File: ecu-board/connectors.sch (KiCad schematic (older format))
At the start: 31 parts, among them J10 Injector connector, J13 Chrankshaft Hall connector, J14 Camshaft Hall connector, J2 Battery power conenctor, J4 Motor conenctor, J5 Serial DB9 connector, J8 IAT connector, J9 CLT connector

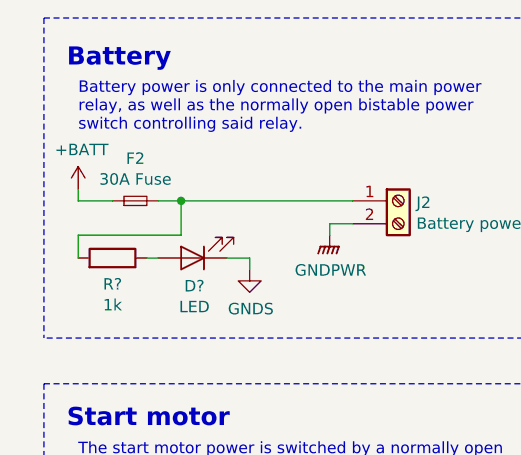
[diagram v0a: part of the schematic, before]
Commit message: Remove main fuse. To be replaced by inline. See #4.
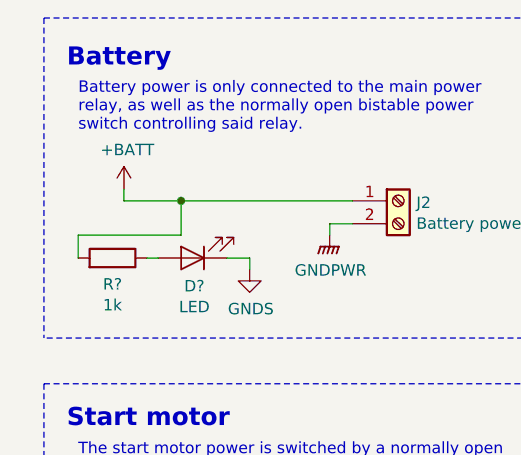
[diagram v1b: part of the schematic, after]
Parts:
- removed F2: 30A Fuse, symbol Device:Fuse_Small
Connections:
- net +BATT: now also J2.1 (Pin_1), R?.2
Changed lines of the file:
@@
 L power:+BATT #PWR06
 U 1 1 5C5D2F4D
-P 950 1650
-F 0 "#PWR06" H 950 1500 50  0001 C CNN
-F 1 "+BATT" H 965 1823 50  0000 C CNN
-F 2 "" H 950 1650 50  0001 C CNN
-F 3 "" H 950 1650 50  0001 C CNN
-	1    950  1650
+P 1150 1650
+F 0 "#PWR06" H 1150 1500 50  0001 C CNN
+F 1 "+BATT" H 1165 1823 50  0000 C CNN
+F 2 "" H 1150 1650 50  0001 C CNN
+F 3 "" H 1150 1650 50  0001 C CNN
+	1    1150 1650
 	1    0    0    -1
 $EndComp
 Wire Wire Line
 	2050 1800 2150 1800
-$Comp
-L Device:Fuse_Small F2
-U 1 1 5C5D4B6E
-P 1200 1700
-F 0 "F2" H 1200 1515 50  0000 C CNN
-F 1 "30A Fuse" H 1200 1606 50  0000 C CNN
-F 2 "" H 1200 1700 50  0001 C CNN
-F 3 "~" H 1200 1700 50  0001 C CNN
-F 4 "2292904" H -5600 -2800 50  0001 C CNN "Farnell"
-	1    1200 1700
-	1    0    0    1
-$EndComp
 Wire Notes Line
 	3400 2300 800  2300
@@
 	1650 3700 1700 3700
 Wire Wire Line
-	950  1650 950  1700
-Wire Wire Line
-	950  1700 1100 1700
+	1150 1650 1150 1700
 Wire Wire Line
 	1900 3300 2000 3300
@@
 	1    0    0    -1
 $EndComp
-Wire Wire Line
-	1300 1700 1400 1700
 $Comp
 L power:GNDS #PWR?
@@
 	1    0    0    -1
 $EndComp
+Wire Wire Line
+	1150 1700 1400 1700
 $EndSCHEMATC

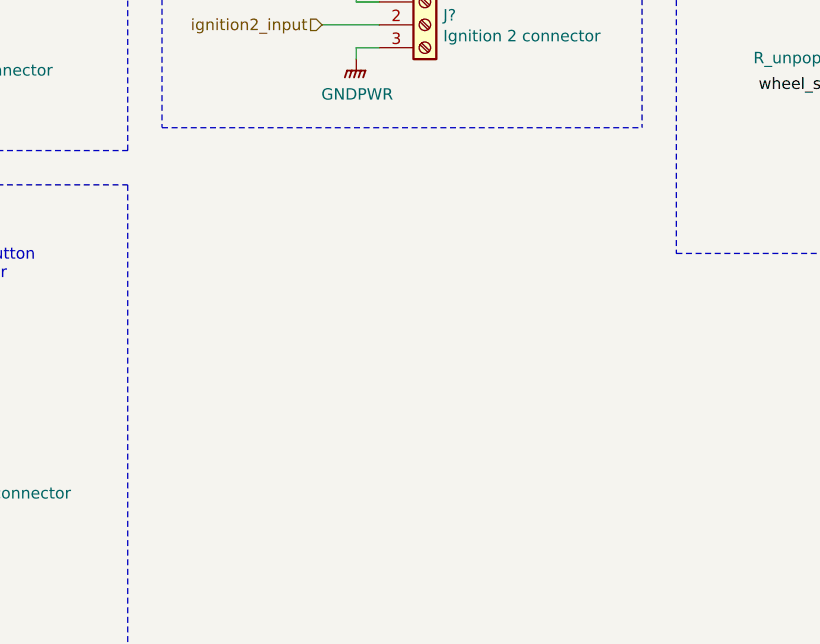
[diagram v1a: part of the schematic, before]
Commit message: Add camera connector. #21.
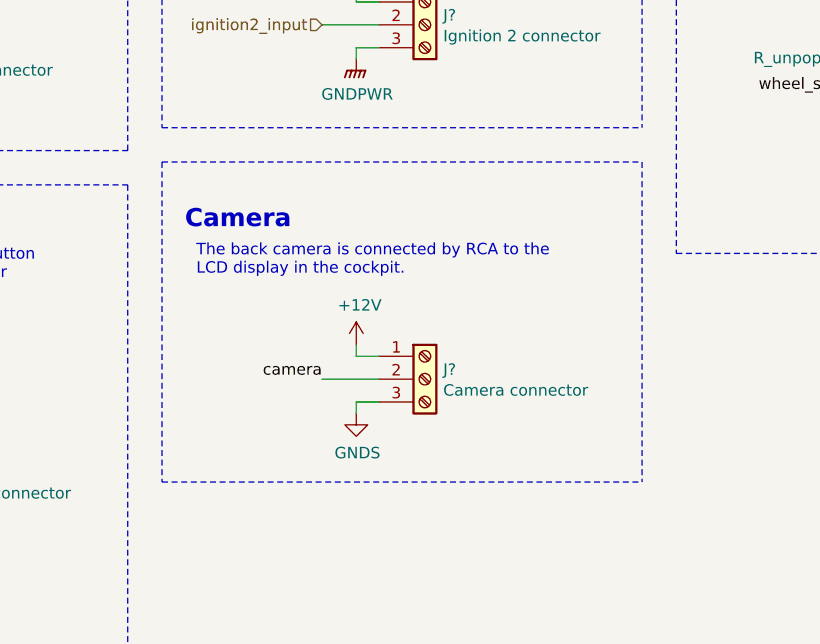
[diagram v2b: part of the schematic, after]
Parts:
- added J?: Camera connector, symbol Connector:Screw_Terminal_01x03
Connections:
- net +12V: now also J?.1 (Pin_1)
- net GNDS: now also J?.3 (Pin_3)
- net camera: now also J?.2 (Pin_2)
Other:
- note added: "Camera\n"
- note added: "The back camera is connected by RCA to the \nLCD display in the cockpit."
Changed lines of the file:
@@
 Wire Wire Line
 	1150 1700 1400 1700
+Text Notes 6200 5100 0    79   ~ 16
+Camera\n
+Wire Notes Line
+	6100 4800 8200 4800
+$Comp
+L Connector:Screw_Terminal_01x03 J?
+U 1 1 5CE57F74
+P 7250 5750
+F 0 "J?" H 7330 5792 50  0000 L CNN
+F 1 "Camera connector" H 7330 5701 50  0000 L CNN
+F 2 "" H 7250 5750 50  0001 C CNN
+F 3 "http://www.farnell.com/datasheets/2308387.pdf?_ga=2.20224184.1892952727.1549112209-881392492.1520553087" H 7250 5750 50  0001 C CNN
+F 4 "2315020, 2315083" H 7250 5750 50  0001 C CNN "Farnell"
+	1    7250 5750
+	1    0    0    -1
+$EndComp
+$Comp
+L power:+12V #PWR?
+U 1 1 5CE589F7
+P 6950 5600
+F 0 "#PWR?" H 6950 5450 50  0001 C CNN
+F 1 "+12V" H 6965 5773 50  0000 C CNN
+F 2 "" H 6950 5600 50  0001 C CNN
+F 3 "" H 6950 5600 50  0001 C CNN
+	1    6950 5600
+	1    0    0    -1
+$EndComp
+Wire Wire Line
+	6950 5600 6950 5650
+Wire Wire Line
+	6950 5650 7050 5650
+$Comp
+L power:GNDS #PWR?
+U 1 1 5CE601B5
+P 6950 5900
+F 0 "#PWR?" H 6950 5650 50  0001 C CNN
+F 1 "GNDS" H 6955 5727 50  0000 C CNN
+F 2 "" H 6950 5900 50  0001 C CNN
+F 3 "" H 6950 5900 50  0001 C CNN
+	1    6950 5900
+	1    0    0    -1
+$EndComp
+Wire Wire Line
+	6950 5900 6950 5850
+Wire Wire Line
+	6950 5850 7050 5850
+Text Label 6800 5750 2    50   ~ 0
+camera
+Wire Wire Line
+	6800 5750 7050 5750
+Text Notes 6250 5300 0    50   ~ 0
+The back camera is connected by RCA to the \nLCD display in the cockpit.
+Wire Notes Line
+	6100 6200 8200 6200
+Wire Notes Line
+	8200 4800 8200 6200
+Wire Notes Line
+	6100 4800 6100 6200
 $EndSCHEMATC

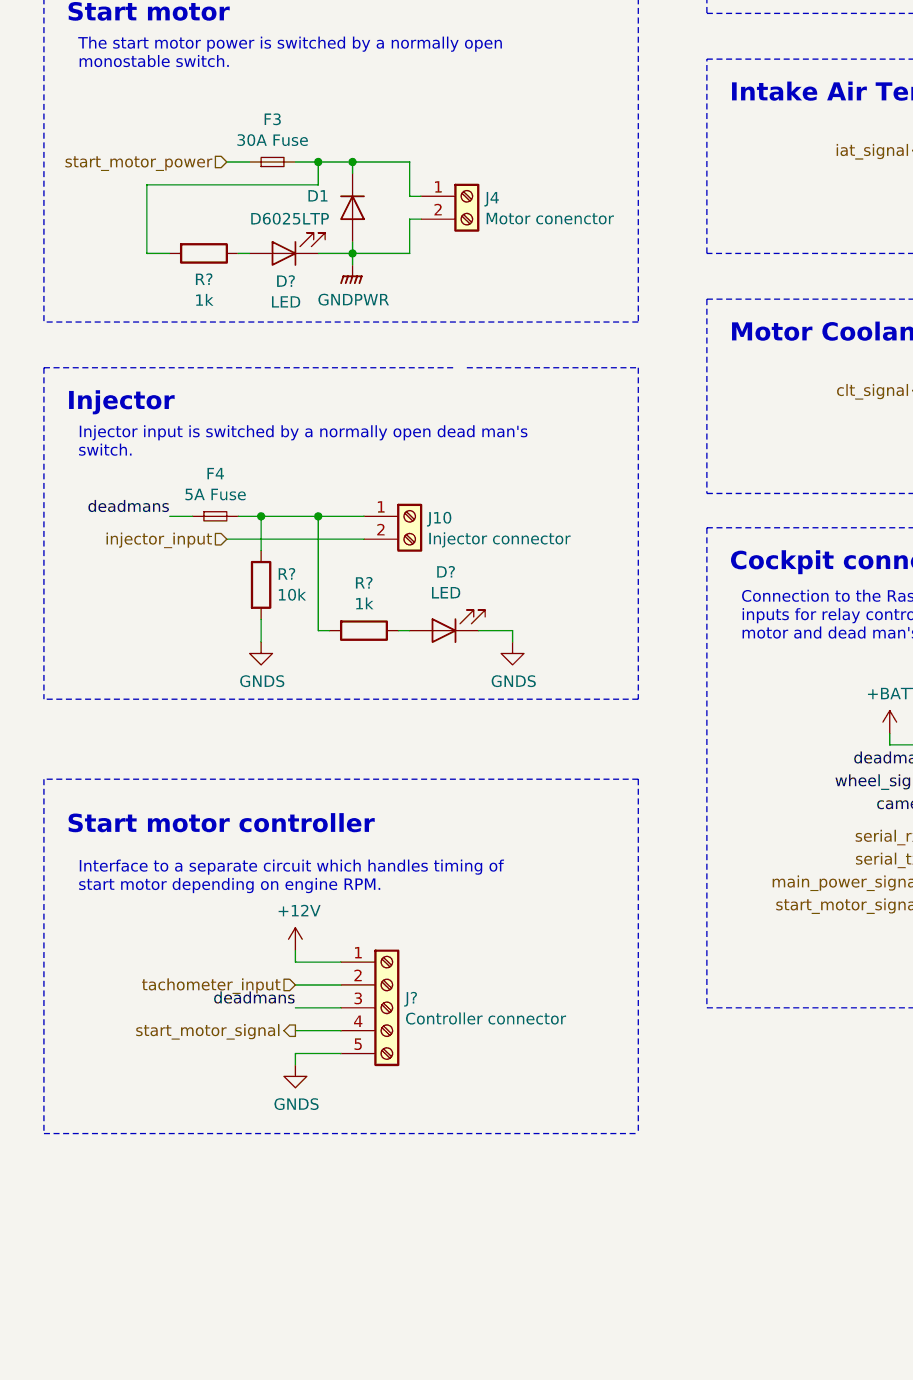
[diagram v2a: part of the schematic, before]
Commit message: Add backlight connector. Resolves #21.
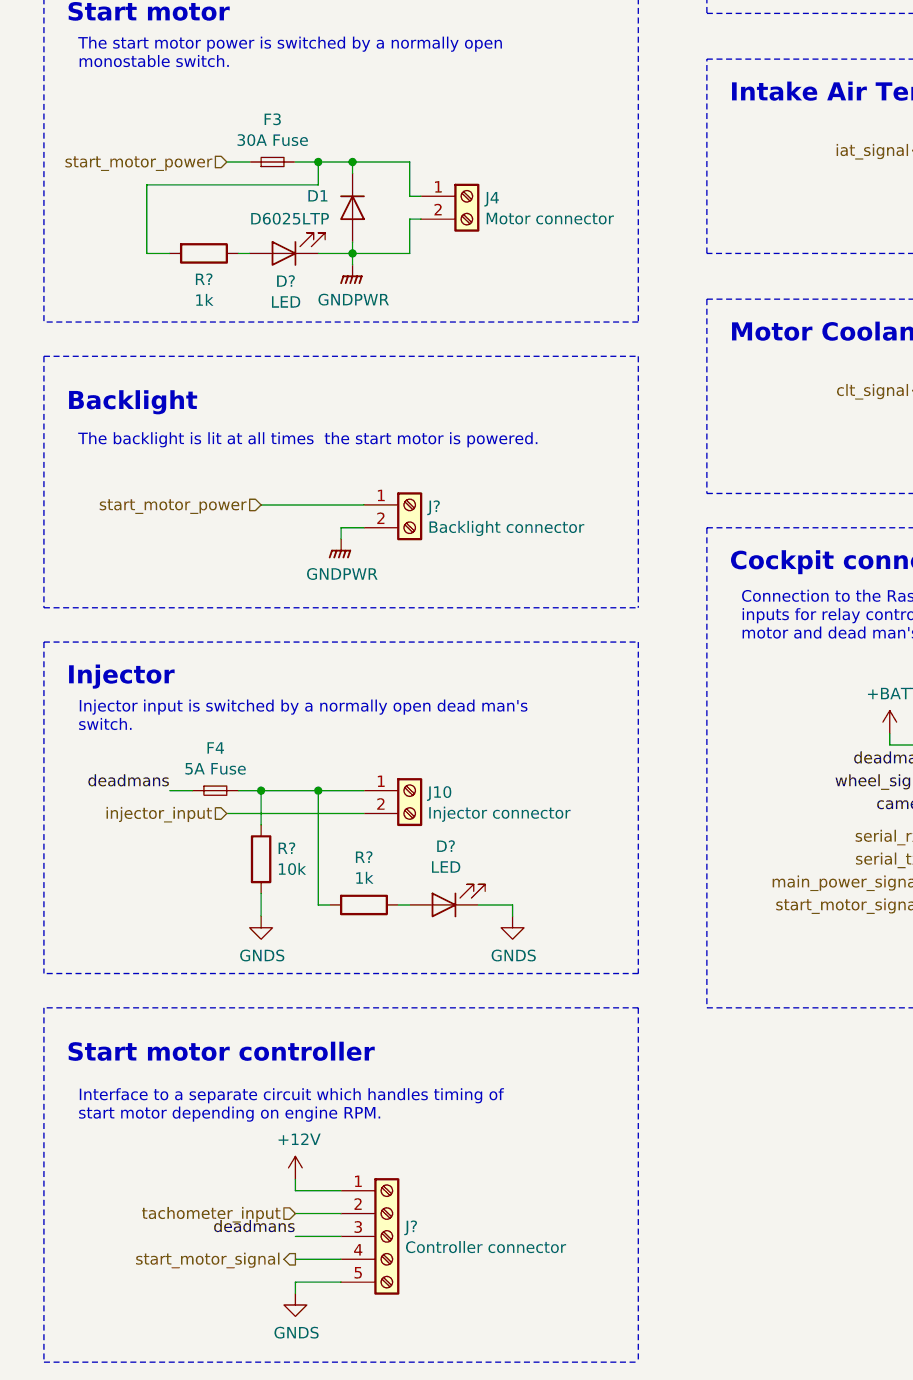
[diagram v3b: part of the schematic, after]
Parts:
- added J?: Backlight connector, symbol Connector:Screw_Terminal_01x02
- J4: value Motor conenctor -> Motor connector
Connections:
- net GNDPWR: now also J?.2 (Pin_2)
- net start_motor_power: now also J?.1 (Pin_1)
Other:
- note added: "Backlight\n"
- note added: "The backlight is lit at all times the start motor is powered."
- moved on the sheet: D?, F4, J10, J?, R?

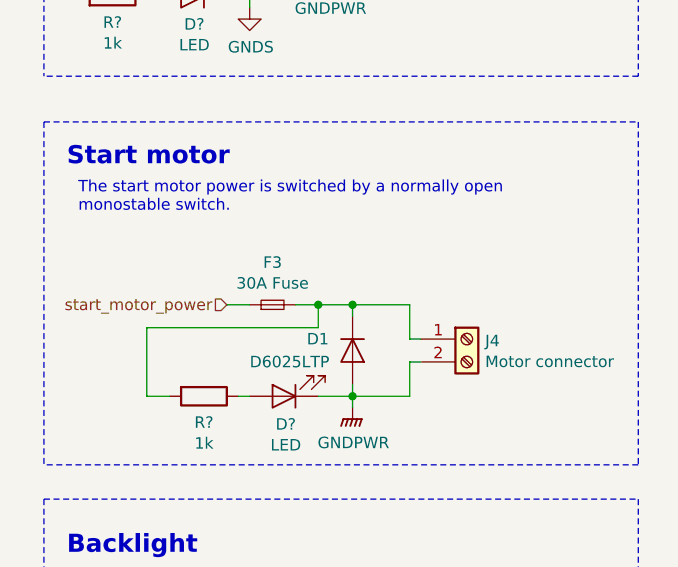
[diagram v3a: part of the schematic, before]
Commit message: Change starter motor fuse to 40A. Closes #30.
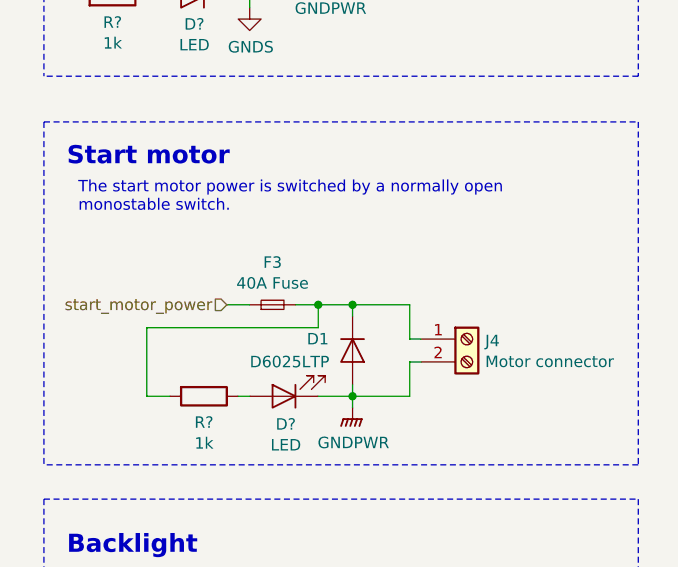
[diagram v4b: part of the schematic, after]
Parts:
- F3: value 30A Fuse -> 40A Fuse
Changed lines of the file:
@@
 P 1800 3300
 F 0 "F3" H 1800 3115 50  0000 C CNN
-F 1 "30A Fuse" H 1800 3206 50  0000 C CNN
+F 1 "40A Fuse" H 1800 3206 50  0000 C CNN
 F 2 "" H 1800 3300 50  0001 C CNN
 F 3 "~" H 1800 3300 50  0001 C CNN

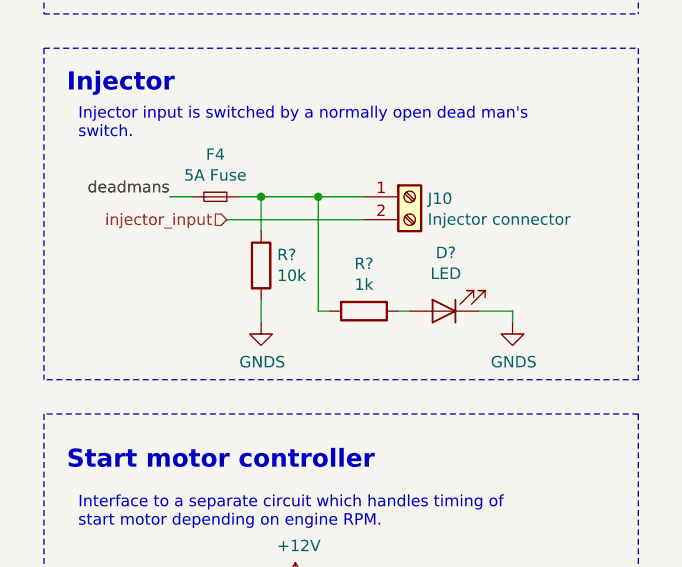
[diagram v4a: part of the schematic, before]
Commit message: Remove unecessary pull-down.
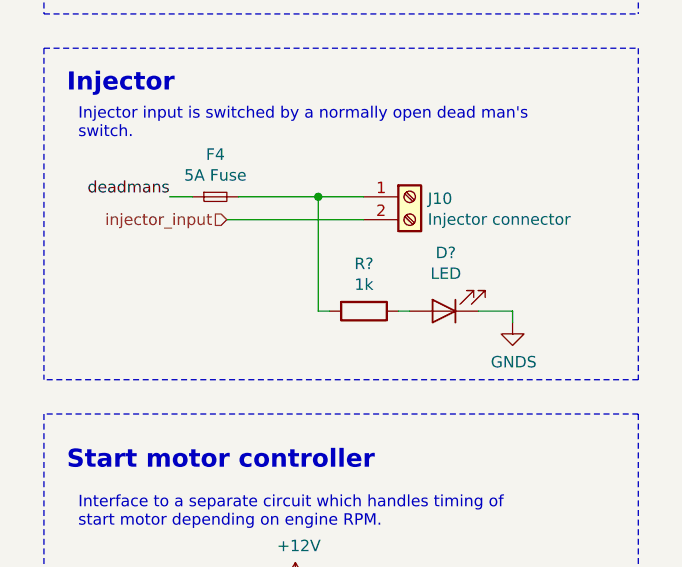
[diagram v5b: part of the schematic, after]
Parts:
- removed R?: 10k, symbol Device:R
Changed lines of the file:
@@
 Wire Notes Line
 	6100 2450 6100 4650
-$Comp
-L power:GNDS #PWR?
-U 1 1 5C783863
-P 1750 6600
-F 0 "#PWR?" H 1750 6350 50  0001 C CNN
-F 1 "GNDS" H 1755 6427 50  0000 C CNN
-F 2 "" H 1750 6600 50  0001 C CNN
-F 3 "" H 1750 6600 50  0001 C CNN
-	1    1750 6600
-	1    0    0    -1
-$EndComp
-$Comp
-L Device:R R?
-U 1 1 5C7A1D9C
-P 1750 6350
-F 0 "R?" H 1820 6396 50  0000 L CNN
-F 1 "10k" H 1820 6305 50  0000 L CNN
-F 2 "" V 1680 6350 50  0001 C CNN
-F 3 "~" H 1750 6350 50  0001 C CNN
-	1    1750 6350
-	1    0    0    -1
-$EndComp
-Wire Wire Line
-	1750 6200 1750 6050
-Wire Wire Line
-	1650 6050 1750 6050
-Connection ~ 1750 6050
 Wire Wire Line
 	1350 6050 1450 6050
@@
 	1600 6150 2200 6150
 Wire Wire Line
-	1750 6050 2000 6050
-Wire Wire Line
-	1750 6500 1750 6600
-Wire Wire Line
 	2050 6550 2000 6550
 Wire Wire Line
@@
 Wire Notes Line
 	3400 4150 3400 5250
+Wire Wire Line
+	1650 6050 2000 6050
 $EndSCHEMATC

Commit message: Change hal connectors from 4 to 3 pin.
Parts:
- J13, J14, J?: symbol Connector:Screw_Terminal_01x04 -> Connector:Screw_Terminal_01x03; Farnell 2315043, 2315064 -> 2315020, 2315083
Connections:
- net GNDS: no longer J13.4 (Pin_4), J14.4 (Pin_4), J?.4 (Pin_4)
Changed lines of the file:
@@
 L power:GNDS #PWR021
 U 1 1 5C570990
-P 9500 2450
-F 0 "#PWR021" H 9500 2200 50  0001 C CNN
-F 1 "GNDS" H 9505 2277 50  0000 C CNN
-F 2 "" H 9500 2450 50  0001 C CNN
-F 3 "" H 9500 2450 50  0001 C CNN
-	1    9500 2450
-	1    0    0    -1
-$EndComp
-Wire Wire Line
-	9500 2450 9500 2400
-Wire Wire Line
-	9500 2400 9600 2400
+P 9500 2400
+F 0 "#PWR021" H 9500 2150 50  0001 C CNN
+F 1 "GNDS" H 9505 2227 50  0000 C CNN
+F 2 "" H 9500 2400 50  0001 C CNN
+F 3 "" H 9500 2400 50  0001 C CNN
+	1    9500 2400
+	1    0    0    -1
+$EndComp
 $Comp
 L power:GNDS #PWR023
 U 1 1 5C5709C2
-P 9500 3600
-F 0 "#PWR023" H 9500 3350 50  0001 C CNN
-F 1 "GNDS" H 9505 3427 50  0000 C CNN
-F 2 "" H 9500 3600 50  0001 C CNN
-F 3 "" H 9500 3600 50  0001 C CNN
-	1    9500 3600
-	1    0    0    -1
-$EndComp
-Wire Wire Line
-	9500 3600 9500 3550
-Wire Wire Line
-	9500 3550 9600 3550
-Wire Wire Line
-	9500 3550 9500 3450
+P 9500 3550
+F 0 "#PWR023" H 9500 3300 50  0001 C CNN
+F 1 "GNDS" H 9505 3377 50  0000 C CNN
+F 2 "" H 9500 3550 50  0001 C CNN
+F 3 "" H 9500 3550 50  0001 C CNN
+	1    9500 3550
+	1    0    0    -1
+$EndComp
 Wire Wire Line
 	9500 3450 9600 3450
-Connection ~ 9500 3550
-Wire Wire Line
-	9500 2400 9500 2300
 Wire Wire Line
 	9500 2300 9600 2300
-Connection ~ 9500 2400
 Text Notes 8500 1450 0    50   ~ 0
 Hall Sensor Model: Littlefuse 55110-3M-03-A\nCrankshaft Sensor: CYKN8-02CL0\nSecond ground is for potential shielding.\nJumpers enable using other hall sensors.
@@
 $EndComp
 $Comp
-L Connector:Screw_Terminal_01x04 J13
+L Connector:Screw_Terminal_01x03 J13
 U 1 1 5C5953F1
 P 9800 2200
@@
 F 2 "" H 9800 2200 50  0001 C CNN
 F 3 "~" H 9800 2200 50  0001 C CNN
-F 4 "2315043, 2315064" H 9800 2200 50  0001 C CNN "Farnell"
+F 4 "2315020, 2315083" H 9800 2200 50  0001 C CNN "Farnell"
 	1    9800 2200
 	1    0    0    -1
 $EndComp
 $Comp
-L Connector:Screw_Terminal_01x04 J14
+L Connector:Screw_Terminal_01x03 J14
 U 1 1 5C596299
 P 9800 3350
@@
 F 2 "" H 9800 3350 50  0001 C CNN
 F 3 "~" H 9800 3350 50  0001 C CNN
-F 4 "2315043, 2315064" H 9800 3350 50  0001 C CNN "Farnell"
+F 4 "2315020, 2315083" H 9800 3350 50  0001 C CNN "Farnell"
 	1    9800 3350
 	1    0    0    -1
@@
 deadmans
 $Comp
-L Connector:Screw_Terminal_01x04 J?
+L Connector:Screw_Terminal_01x03 J?
 U 1 1 5C788398
 P 9800 4500
@@
 F 2 "" H 9800 4500 50  0001 C CNN
 F 3 "~" H 9800 4500 50  0001 C CNN
-F 4 "2315043, 2315064" H 9800 4500 50  0001 C CNN "Farnell"
+F 4 "2315020, 2315083" H 9800 4500 50  0001 C CNN "Farnell"
 	1    9800 4500
 	1    0    0    -1
@@
 L power:GNDS #PWR?
 U 1 1 5C78841E
-P 9500 4800
-F 0 "#PWR?" H 9500 4550 50  0001 C CNN
-F 1 "GNDS" H 9505 4627 50  0000 C CNN
-F 2 "" H 9500 4800 50  0001 C CNN
-F 3 "" H 9500 4800 50  0001 C CNN
-	1    9500 4800
+P 9500 4700
+F 0 "#PWR?" H 9500 4450 50  0001 C CNN
+F 1 "GNDS" H 9505 4527 50  0000 C CNN
+F 2 "" H 9500 4700 50  0001 C CNN
+F 3 "" H 9500 4700 50  0001 C CNN
+	1    9500 4700
 	1    0    0    -1
 $EndComp
@@
 Wire Wire Line
 	9600 4600 9500 4600
-Wire Wire Line
-	9500 4600 9500 4700
-Wire Wire Line
-	9600 4700 9500 4700
-Connection ~ 9500 4700
-Wire Wire Line
-	9500 4700 9500 4800
 Text Label 4700 6050 2    50   ~ 0
 wheel_signal
@@
 Wire Wire Line
 	1650 6050 2000 6050
+Wire Wire Line
+	9500 4700 9500 4600
+Wire Wire Line
+	9500 3550 9500 3450
+Wire Wire Line
+	9500 2400 9500 2300
 $EndSCHEMATC
